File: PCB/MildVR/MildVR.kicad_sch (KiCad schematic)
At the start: 8 parts, among them J1 WP7B-S040VA1-R6000, J2 WP7B-S040VA1-R6000, J3 20539-050E-01, J4 20539-050E-01, U1 ESP32-S3, U2 HMC6301BG46, U3 BMI270, U4 BMI270

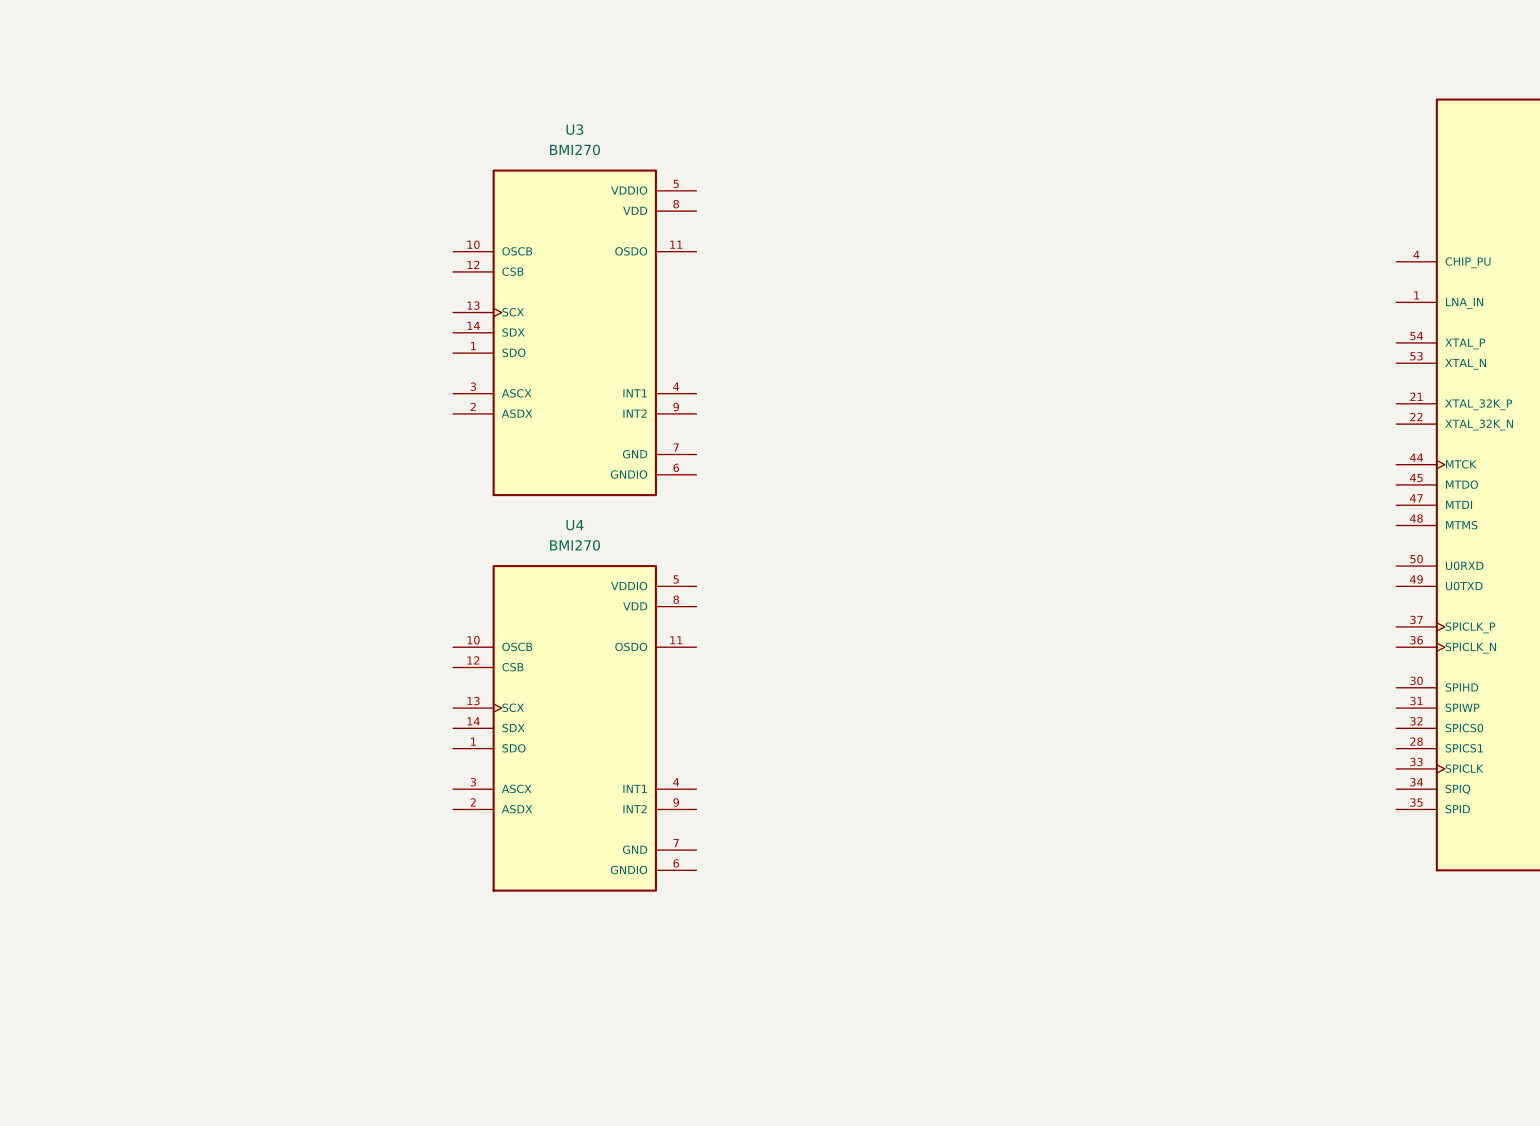
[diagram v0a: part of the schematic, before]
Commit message: Begin wiring of BMI270s
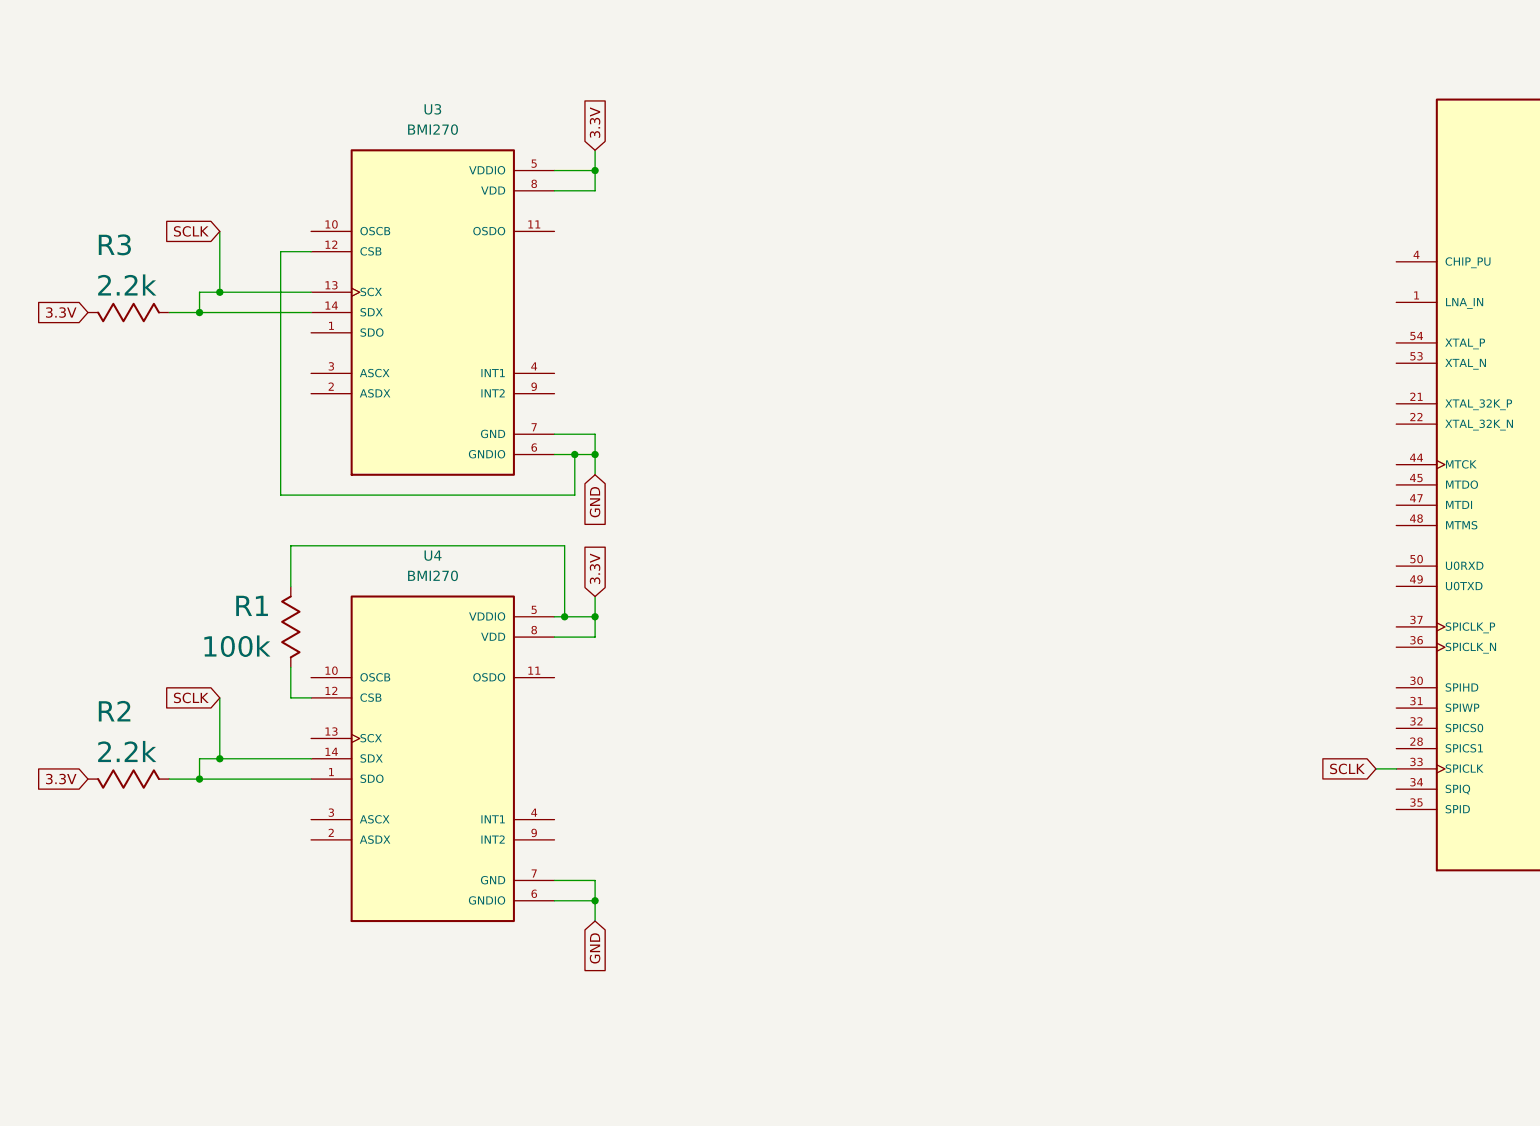
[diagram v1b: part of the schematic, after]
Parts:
- added R1: 100k, symbol PCM_Generic:R,IEEE
- added R2, R3: 2.2k, symbol PCM_Generic:R,IEEE
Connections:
- net SCLK: now reaches U4.1 (SDO)
- net SCLK: now also U1.33 (SPICLK), U3.13 (SCX), U3.14 (SDX), U4.14 (SDX), R2.1 (+), R3.1 (+)
- net at U4.12 (CSB): now also R1.2 (-)
- net 3.3V: now reaches U4.5 (VDDIO)
- net 3.3V: now also U3.5 (VDDIO), U3.8 (VDD), U4.8 (VDD), R1.1 (+), R2.2 (-), R3.2 (-)
- net GND: now reaches U4.6 (GNDIO)
- net GND: now also U3.12 (CSB), U3.6 (GNDIO), U3.7 (GND), U4.7 (GND)
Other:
- moved on the sheet: U3, U4

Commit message: [PCB] Routing Gyros and Receiver power
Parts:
- removed R1: 100k, symbol PCM_Generic:R,IEEE
- removed R2, R3: 2.2k, symbol PCM_Generic:R,IEEE
- added C1: 10nF, Capacitor_THT:C_Disc_D3.0mm_W2.0mm_P2.50mm, symbol PCM_SL_Devices:Capacitor_NP
- added C2, C3, C4, C5: 100nF, Capacitor_THT:C_Disc_D3.0mm_W2.0mm_P2.50mm, symbol PCM_SL_Devices:Capacitor_NP
- added C6, C7, C8, C9: 1uF, Capacitor_THT:C_Disc_D3.0mm_W2.0mm_P2.50mm, symbol PCM_SL_Devices:Capacitor_NP
- added PS1, PS2: AP7365-WG-7, AP7365-WG-7:AP7365-WG-7, symbol AP7365-WG-7:AP7365-WG-7
- added R1, R2, R3: 4.7k, symbol PCM_Generic-50:R,IEEE
- added R4: 2k, symbol PCM_Generic-50:R,IEEE
- added R5: 2.7k, symbol PCM_Generic-50:R,IEEE
- added R6: 4k, symbol PCM_Generic-50:R,IEEE
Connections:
- net 3.3V: now also U1.2 (VDD3P3), U1.3 (VDD3P3), U3.1 (SDO), U3.12 (CSB), U4.12 (CSB), C1.1, C2.2, C3.2, C4.2, C5.2, C6.2, C8.2, PS1.1 (IN), PS1.3 (EN), PS2.1 (IN), PS2.3 (EN), R1.1 (+), R2.1 (+)
- net GND: now also U1.57 (GND), U2.B3 (GND), U2.B4 (GND), U2.B6 (GND), U2.B7 (GND), U2.C1 (GND), U2.C2 (GND), U2.C3 (GND), U2.C4 (GND), U2.C5 (GND), U2.C6 (GND), U2.D1 (GND), U2.D6 (GND), U2.D7 (GND), U2.D8 (GND), U2.F1 (GND), U2.G2 (GND), U2.G4 (GND), U2.H1 (GND), U2.H5 (GND), U4.1 (SDO), C1.2, C2.1, C3.1, C4.1, C5.1, C6.1, C7.1, C8.1, C9.1, PS1.2 (GND), PS2.2 (GND), R4.1 (+), R6.1 (+); no longer U3.12 (CSB)
- net at U4.13 (SCX): now also U1.6 (GPIO1), U3.13 (SCX), R1.2 (-)
- net at U1.5 (GPIO0): now also U3.14 (SDX), U4.14 (SDX), R2.2 (-)
- net at U2.A10 (VCCDIV): now also U2.A11 (VCCDIV), U2.A12 (VCCDIV), U2.A5 (VCCBUF), U2.A9 (VCCDIV), U2.B10 (VCCDIV), U2.B11 (VCCDIV), U2.B12 (VCCDIV), U2.C10 (VSSDIV), U2.C11 (VSSDIV), U2.C12 (VSSDIV), U2.C9 (VSSDIV), U2.G10 (VCCVCO), U2.G3 (VCCMIX), U2.G5 (VCCTRIP), U2.G7 (VSSVCO), U2.G8 (VSSVCO), U2.G9 (VCCVCO), U2.H10 (VSSVCO), U2.H11 (VSSVCO), U2.H12 (VSSVCO), U2.H3 (VCCIF), U2.H6 (VSSVCO), U2.H9 (VSSVCO), C7.2, PS1.5 (OUT), R3.2 (-)
- net at U2.B5 (VDDD): now also U2.F9 (VDDSYN), U2.G12 (VDDSYN), C9.2, PS2.5 (OUT), R5.2 (-)
- net at U2.D10 (VSSLPF): now also U2.D11 (VSSLPF), U2.D12 (VSSLPF), U2.D9 (VSSLPF)
- net at U2.E10 (VSSCP): now also U2.E11 (VSSCP)
- net at U2.F10 (VSSREF): now also U2.F11 (VSSREF)
- removed net SCLK: U1.33 (SPICLK), U3.13 (SCX), U3.14 (SDX), U4.1 (SDO), U4.14 (SDX)
- new net: PS2.4 (ADJ), R5.1 (+), R6.2 (-)
- new net: PS1.4 (ADJ), R3.1 (+), R4.2 (-)
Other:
- note added: "1.35V"
- note added: "2.7V"

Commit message: [PCB] Reciever Setup Routing + Organization
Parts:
- added C10, C11: 1uF, Capacitor_THT:C_Disc_D3.0mm_W2.0mm_P2.50mm, symbol PCM_SL_Devices:Capacitor_NP
- added C12, C14, C21, C22: 1F, Capacitor_THT:C_Disc_D3.0mm_W2.0mm_P2.50mm, symbol PCM_SL_Devices:Capacitor_NP
- added C13, C15, C16, C17, C18, C19, C20: 1nF, Capacitor_THT:C_Disc_D3.0mm_W2.0mm_P2.50mm, symbol PCM_SL_Devices:Capacitor_NP
- added C23, C25: 100nF, Capacitor_THT:C_Disc_D3.0mm_W2.0mm_P2.50mm, symbol PCM_SL_Devices:Capacitor_NP
- added C24: 100pF, Capacitor_THT:C_Disc_D3.0mm_W2.0mm_P2.50mm, symbol PCM_SL_Devices:Capacitor_NP
- added PS3: AP7365-WG-7, AP7365-WG-7:AP7365-WG-7, symbol AP7365-WG-7:AP7365-WG-7
- added Q1: BSS138, BSS138:SOT95P240X111-3N, symbol BSS138:BSS138
- added R10, R12, R14, R15, R16, R17: 1.2k, symbol PCM_Generic-50:R,IEEE
- added R11, R13, R9: 2.2k, symbol PCM_Generic-50:R,IEEE
- added R7: 2k, symbol PCM_Generic-50:R,IEEE
- added R8: 1k, symbol PCM_Generic-50:R,IEEE
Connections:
- net 3.3V: now also C10.2, PS3.1 (IN), PS3.3 (EN), Q1.2
- net GND: now also C10.1, C11.1, C12.1, C13.2, C14.1, C15.1, C16.2, C17.1, C18.1, C19.1, C20.1, C23.2, C25.1, PS3.2 (GND), R10.2 (-), R12.2 (-), R14.2 (-), R7.1 (+)
- net 1.35V: now reaches C9.2, PS2.5 (OUT), R5.2 (-), U2.B5 (VDDD), U2.F9 (VDDSYN), U2.G12 (VDDSYN)
- net 1.35V: now also U2.A10 (VCCDIV), U2.A11 (VCCDIV), U2.A12 (VCCDIV), U2.A9 (VCCDIV), U2.B10 (VCCDIV), U2.B11 (VCCDIV), U2.B12 (VCCDIV), U2.C10 (VSSDIV), U2.C11 (VSSDIV), U2.C12 (VSSDIV), U2.C9 (VSSDIV), U2.G10 (VCCVCO), U2.G3 (VCCMIX), U2.G5 (VCCTRIP), U2.G7 (VSSVCO), U2.G8 (VSSVCO), U2.G9 (VCCVCO), U2.H10 (VSSVCO), U2.H11 (VSSVCO), U2.H12 (VSSVCO), U2.H2 (VCOLNA), U2.H3 (VCCIF), U2.H6 (VSSVCO), U2.H9 (VSSVCO), C12.2, C13.1, C14.2, C15.2, C16.1, C17.2, C18.2, C19.2
- net SPICLK: now reaches U1.33 (SPICLK)
- net SPICLK: now also R9.1 (+)
- net at U1.43 (GPIO38): now also Q1.3
- net at U1.51 (GPIO45): now also R13.1 (+)
- net at U1.52 (GPIO46): now also R11.1 (+)
- net at U2.A1 (CLK): now also R10.1 (+), R9.2 (-)
- net at U2.A2 (SCANOUT): now also Q1.1, R15.2 (-)
- net at U2.B1 (ENABLE): now also R11.2 (-), R12.1 (+)
- net at U2.B2 (DATA): now also R13.2 (-), R14.1 (+)
- net at U2.B8 (EXTFIL_P): now also C21.2, R17.1 (+)
- net at U2.B9 (EXTFIL_N): now also C21.1, R16.2 (-)
- net at U2.G11 (VCCRCAP): now also C23.1, C24.2
- net at U2.G6 (VREGOUT): now also C24.1, C25.2
- new net: C22.2, R17.2 (-)
- new net: PS3.4 (ADJ), R7.2 (-), R8.1 (+)
- new net: C22.1, R16.1 (+)
- new net 1.2V: C11.2, PS3.5 (OUT), R15.1 (+), R8.2 (-)
- new net 2.7V: C20.2, C7.2, PS1.5 (OUT), R3.2 (-), U2.A5 (VCCBUF)
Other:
- note removed: "1.35V"
- note removed: "2.7V"
- moved on the sheet: C6, C7, PS1, R3, R4

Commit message: [PCB] Replace ESP32-S3 with Raspbery Pi CM4
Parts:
- removed J3, J4: 20539-050E-01, 20539-050E-01:IPEX_20539-050E-01, symbol (CSI) 20539-050E-01:20539-050E-01
- removed U1: ESP32-S3, ESP32-S3:ESP32-S3, symbol ESP32-S3:ESP32-S3
- added J3: CAM1, ZF5S-15-03-T-WT:SAMTEC_ZF5S-15-03-T-WT, symbol ZF5S-15-03-T-WT:ZF5S-15-03-T-WT
- added J4: CAM2, ZF5S-15-03-T-WT:SAMTEC_ZF5S-15-03-T-WT, symbol ZF5S-15-03-T-WT:ZF5S-15-03-T-WT
- added J5: GPIO, DF40C-100DS-0.4V_51:HIROSE_DF40C-100DS-0.4V_51_, symbol DF40C-100DS-0.4V_51:DF40C-100DS-0.4V_51_
- added J6: High Speed Serial, DF40C-100DS-0.4V_51:HIROSE_DF40C-100DS-0.4V_51_, symbol DF40C-100DS-0.4V_51:DF40C-100DS-0.4V_51_
- added R18: 1k, symbol PCM_Generic-50:R,IEEE
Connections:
- net 3.3V: now also J3.15, J4.15, R18.1 (+)
- net SDA: now reaches R2.2 (-), U3.14 (SDX), U4.14 (SDX)
- net SDA: now also J5.58
- net REN: now reaches R11.1 (+)
- net CLK: now reaches R1.2 (-), U3.13 (SCX), U4.13 (SCX)
- net CLK: now also J5.56
- net MISO: now reaches Q1.3
- net MOSI: now reaches R13.1 (+)
- net GND renamed P,GND
- net P,GND: now also J3.01, J3.04, J3.07, J3.10, J4.01, J4.04, J4.07, J4.10, J5.1, J5.13, J5.14, J5.2, J5.22, J5.23, J5.32, J5.33, J5.42, J5.43, J5.52, J5.53, J5.59, J5.60, J5.65, J5.66, J5.7, J5.71, J5.74, J5.8, J5.98, J6.13, J6.14, J6.19, J6.20, J6.25, J6.26, J6.31, J6.32, J6.37, J6.38, J6.44, J6.50, J6.55, J6.56, J6.61, J6.62, J6.67, J6.68, J6.7, J6.73, J6.74, J6.79, J6.8, J6.80, J6.85, J6.86, J6.91, J6.92, J6.97, J6.98; no longer C13.2, C6.1, C8.1, U2.H1 (GND), U2.H5 (GND)
- net SPICLK renamed SCLK
- new net: J4.02, J6.15
- new net: J4.03, J6.17
- new net: J4.05, J6.21
- new net: J4.06, J6.23
- new net: J4.08, J6.27
- new net: J3.02, J6.28
- new net: J4.09, J6.29
- new net: J3.03, J6.30
- new net: J3.05, J6.34
- new net: J3.06, J6.36
- new net: J3.08, J6.40
- new net: J3.09, J6.42
- new net: J5.21, R18.2 (-)
- new net: U2.H1 (GND), U2.H5 (GND)
- new net 1V8: J5.88, J5.90
- new net 3V3: J5.84, J5.86
- new net 5V: J5.77, J5.79, J5.81, J5.83, J5.85, J5.87
- new net AIN0: J5.96
- new net AIN1: J5.94
- new net CAM1_D2_N: J6.33
- new net CAM1_D2_P: J6.35
- new net CAM1_D3_N: J6.39
- new net CAM1_D3_P: J6.41
- new net CAM_GPIO: J3.11, J4.11, J5.97
- new net DSI0_C_N: J6.69
- new net DSI0_C_P: J6.71
- new net DSI0_D0_N: J6.57
- new net DSI0_D0_P: J6.59
- new net DSI0_D1_N: J6.63
- new net DSI1_C_N: J6.87
- new net DSI1_C_P: J6.89
- new net DSI1_D0_N: J6.75
- new net DSI1_D0_P: J6.77
- new net DSI1_D1_N: J6.81
- new net DSI1_D1_P: J6.83
- new net DSI1_D2_N: J6.93
- new net DSI1_D2_P: J6.95
- new net DSI1_D3_N: J6.94
- new net DSI_D1_P: J6.65
- new net DSI_D3_P: J6.96
- new net EEPROM_nWP: J5.20
- new net ETH_LEDG: J5.17
- new net ETH_LEDY: J5.15
- new net GLOBAL_EN: J5.99
- new net GPIO10: J5.44
- new net GPIO11: J5.38
- new net GPIO12: J5.31
- new net GPIO13: J5.28
- new net GPIO14: J5.55
- new net GPIO15: J5.51
- new net GPIO16: J5.29
- new net GPIO17: J5.50
- new net GPIO18: J5.49
- new net GPIO19: J5.26
- new net GPIO20: J5.27
- new net GPIO21: J5.25
- new net GPIO22: J5.46
- new net GPIO23: J5.47
- new net GPIO24: J5.45
- new net GPIO25: J5.41
- new net GPIO26: J5.24
- new net GPIO27: J5.48
- new net GPIO4: J5.54
- new net GPIO5: J5.34
- new net GPIO6: J5.30
- new net GPIO7: J5.37
- new net GPIO8: J5.39
- new net GPIO9: J5.40
- new net GPIO_VREF: J5.78
- new net HDMI0_CEC: J6.51
- new net HDMI0_CK_N: J6.90
- new net HDMI0_CK_P: J6.88
- new net HDMI0_D0_N: J6.84
- new net HDMI0_D0_P: J6.82
- new net HDMI0_D1_N: J6.78
- new net HDMI0_D1_P: J6.76
- new net HDMI0_D2_N: J6.72
- new net HDMI0_D2_P: J6.70
- new net HDMI0_HOTPLUG: J6.53
- new net HDMI0_SCL: J6.100
- new net HDMI0_SDA: J6.99
- new net HDMI1_CEC: J6.49
- new net HDMI1_CK_N: J6.66
- new net HDMI1_CK_P: J6.64
- new net HDMI1_D0_N: J6.60
- new net HDMI1_D0_P: J6.58
- new net HDMI1_D1_N: J6.54
- new net HDMI1_D1_P: J6.52
- new net HDMI1_D2_N: J6.48
- new net HDMI1_D2_P: J6.46
- new net HDMI1_HOTPLUG: J6.43
- new net HDMI1_SCL: J6.47
- new net HGMI1_SDA: J6.45
- new net ID_SC: J5.35
- new net ID_SD: J5.36
- new net PCIE_CLK_N: J6.12
- new net PCIE_CLK_P: J6.10
- new net PCIE_CLK_nREQ: J6.2
- new net PCIE_RX_N: J6.18
- new net PCIE_RX_P: J6.16
- new net PCIE_TX_N: J6.24
- new net PCIE_nRST: J6.9
- new net PICE_TX_P: J6.22
- new net RUN_PG: J5.92
- new net Reserved: J5.76
- new net SCL0: J3.13, J5.80
- new net SCL1: J4.13
- new net SDA0: J3.14, J5.82
- new net SDA1: J4.14
- new net SD_CLK: J5.57
- new net SD_CMD: J5.62
- new net SD_DAT0: J5.63
- new net SD_DAT1: J5.67
- new net SD_DAT2: J5.69
- new net SD_DAT3: J5.61
- new net SD_PWR_ON: J5.75
- new net SYNC_IN: J5.16
- new net SYNC_OUT: J5.18
- new net TRD0_N: J5.10
- new net TRD0_P: J5.12
- new net TRD1_N: J5.6
- new net TRD1_P: J5.4
- new net TRD2_N: J5.9
- new net TRD2_P: J5.11
- new net TRD3_N: J5.5
- new net TRD3_P: J5.3
- new net TV_OUT: J6.11
- new net USB2_N: J6.3
- new net USB2_P: J6.5
- new net USBOTG_ID: J6.1
- new net nEXTRST: J5.100
- new net nPWER_LED: J5.95
- new net nPWR_LED: J5.93
- new net nRPIBOOT: J5.91
- no-connect marks 0 -> 10
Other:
- moved on the sheet: C1, C10, C11, C12, C13, C14, C15, C16, C17, C18, C19, C2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

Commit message: Organization and stuff
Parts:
- removed C1: 10nF, Capacitor_THT:C_Disc_D3.0mm_W2.0mm_P2.50mm, symbol PCM_SL_Devices:Capacitor_NP
- removed C10, C11, C6, C7, C8, C9: 1uF, Capacitor_THT:C_Disc_D3.0mm_W2.0mm_P2.50mm, symbol PCM_SL_Devices:Capacitor_NP
- removed C12, C14, C21, C22: 1F, Capacitor_THT:C_Disc_D3.0mm_W2.0mm_P2.50mm, symbol PCM_SL_Devices:Capacitor_NP
- removed C13, C15, C16, C17, C18, C19, C20: 1nF, Capacitor_THT:C_Disc_D3.0mm_W2.0mm_P2.50mm, symbol PCM_SL_Devices:Capacitor_NP
- removed C2, C23, C25, C3, C4, C5: 100nF, Capacitor_THT:C_Disc_D3.0mm_W2.0mm_P2.50mm, symbol PCM_SL_Devices:Capacitor_NP
- removed C24: 100pF, Capacitor_THT:C_Disc_D3.0mm_W2.0mm_P2.50mm, symbol PCM_SL_Devices:Capacitor_NP
- added C1: 10nF, GRM022C81C103ME01L(10nF):GRM022C81C222KE01L, symbol PCM_Generic-50:C,IEC
- added C10, C11, C6, C7, C8, C9: 1uF, C0805J105K4RACAUTO(1uF):C0805, symbol PCM_Generic-50:C,IEC
- added C12, C13, C14, C15, C16, C17, C18, C19, C20, C21, C22: 1nF, C1005NP01H102J050BA(1nF):CAPC1005X55N, symbol PCM_Generic-50:C,IEC
- added C2, C3, C4: 100nF, ESR01MZPF4701(4.7k):RESC1005X40N, symbol PCM_Generic-50:C,IEC
- added C23, C25: 100nF, C1005NP01H102J050BA(1nF):CAPC1005X55N, symbol PCM_Generic-50:C,IEC
- added C24: 100pF, symbol PCM_Generic-50:C,IEC
- added C5: 100nF, KAF21BR71H104JM(100nF):CAPC2012X94L, symbol PCM_Generic-50:C,IEC
- added D1: Green, symbol Device:LED
- R1, R2, R3: footprint (none) -> ESR01MZPF4701(4.7k):RESC1005X40N
- U2: footprint BF-75-1_ADI -> HMC6301BG46:HMC6301BG46
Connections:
- net 3.3V is gone; now on net 3V3: J3.15, J4.15, PS1.1 (IN), PS1.3 (EN), PS2.1 (IN), PS2.3 (EN), PS3.1 (IN), PS3.3 (EN), Q1.2, R1.1 (+), R18.1 (+), R2.1 (+), U3.1 (SDO), U3.12 (CSB), U3.5 (VDDIO), U3.8 (VDD), U4.12 (CSB), U4.5 (VDDIO), U4.8 (VDD)
- net P,GND is gone; now on net GND: J3.01, J3.04, J3.07, J3.10, J4.01, J4.04, J4.07, J4.10, J5.1, J5.13, J5.14, J5.2, J5.22, J5.23, J5.32, J5.33, J5.42, J5.43, J5.52, J5.53, J5.59, J5.60, J5.65, J5.66, J5.7, J5.71, J5.74, J5.8, J5.98, J6.13, J6.14, J6.19, J6.20, J6.25, J6.26, J6.31, J6.32, J6.37, J6.38, J6.44, J6.50, J6.55, J6.56, J6.61, J6.62, J6.67, J6.68, J6.7, J6.73, J6.74, J6.79, J6.8, J6.80, J6.85, J6.86, J6.91, J6.92, J6.97, J6.98, PS1.2 (GND), PS2.2 (GND), PS3.2 (GND), R10.2 (-), R12.2 (-), R14.2 (-), R4.1 (+), R6.1 (+), R7.1 (+), U2.B3 (GND), U2.B4 (GND), U2.B6 (GND), U2.B7 (GND), U2.C1 (GND), U2.C2 (GND), U2.C3 (GND), U2.C4 (GND), U2.C5 (GND), U2.C6 (GND), U2.D1 (GND), U2.D6 (GND), U2.D7 (GND), U2.D8 (GND), U2.F1 (GND), U2.G2 (GND), U2.G4 (GND), U3.6 (GNDIO), U3.7 (GND), U4.1 (SDO), U4.6 (GNDIO), U4.7 (GND)
- net 1.2V: now also C11.2 (-)
- net 1.35V: now also C12.2 (-), C13.1 (+), C14.2 (-), C15.1 (+), C16.1 (+), C17.2 (-), C18.2 (-), C19.2 (-), C9.2 (-)
- net 2.7V: now also C20.1 (+), C7.2 (-)
- net 3V3: now also C1.2 (-), C10.2 (-), C2.1 (+), C3.2 (-), C4.1 (+), C5.1 (+), C6.2 (-), C8.2 (-)
- net CAM1_D0_N: now reaches J4.02, J6.15
- net CAM1_D0_P: now reaches J4.03, J6.17
- net CAM1_D1_N: now reaches J4.05, J6.21
- net CAM1_C_P: now reaches J4.06
- net CAM1_C_P: now also J4.08, J4.09, J6.29; no longer J6.23
- net CAM1_C_N: now reaches J6.27
- net CAM1_C_N: no longer J4.08
- net CAM0_D0_N: now reaches J3.02, J6.28
- net CAM0_D0_P: now reaches J3.03, J6.30
- net CAM0_D1_N: now reaches J3.05, J6.34
- net CAM0_D1_P: now reaches J3.06, J6.36
- net CAM0_D1_P: now also J3.08
- net CAM0_C_N: now reaches J6.40
- net CAM0_C_N: no longer J3.08
- net CAM0_C_P: now reaches J3.09, J6.42
- net at U2.G6 (VREGOUT): now also C24.1 (+), C25.2 (-)
- net at U2.G11 (VCCRCAP): now also C23.1 (+), C24.2 (-)
- net at R18.2 (-): now also D1.2 (A); no longer J5.21
- net at R17.1 (+), U2.B8 (EXTFIL_P): now also C21.2 (-)
- net at R17.2 (-): now also C22.2 (-)
- net at R16.1 (+): now also C22.1 (+)
- net at R16.2 (-), U2.B9 (EXTFIL_N): now also C21.1 (+)
- net GND: now reaches U2.H1 (GND), U2.H5 (GND)
- net GND: now also C1.1 (+), C10.1 (+), C11.1 (+), C12.1 (+), C13.2 (-), C14.1 (+), C15.2 (-), C16.2 (-), C17.1 (+), C18.1 (+), C19.1 (+), C2.2 (-), C20.2 (-), C23.2 (-), C25.1 (+), C3.1 (+), C4.2 (-), C5.2 (-), C6.1 (+), C7.1 (+), C8.1 (+), C9.1 (+)
- new net: D1.1 (K), J5.21
- new net CAM1_D1_P: J6.23
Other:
- added sheet Right Controler (Right_Controller.kicad_sch)
- moved on the sheet: J1, J2, PS1, PS2, PS3, Q1, R1, R10, R11, R12, R13, R14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
